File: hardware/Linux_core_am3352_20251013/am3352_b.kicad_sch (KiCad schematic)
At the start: 1 part, among them U1 AM3352BZCZ100

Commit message: update
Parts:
- added C22: 0.1uF, symbol Device:C_Small
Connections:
- net MCASP0_ACLKX: now reaches U1.A13 (MCASP0_ACLKX)
- net MCASP0_AHCLKX: now reaches U1.A14 (MCASP0_AHCLKX)
- net SPI0_CS0: now reaches U1.A16 (SPI0_CS0)
- net SPI0_SCLK: now reaches U1.A17 (SPI0_SCLK)
- net AIN3: now reaches U1.A7 (AIN3)
- net AIN6: now reaches U1.A8 (AIN6)
- net GND: now reaches U1.A9 (VREFN)
- net GND: now also C22.2
- net MCASP0_ACLKR: now reaches U1.B12 (MCASP0_ACLKR)
- net MCASP0_FSX: now reaches U1.B13 (MCASP0_FSX)
- net SPI0_D1: now reaches U1.B16 (SPI0_D1)
- net SPI0_D0: now reaches U1.B17 (SPI0_D0)
- net AIN0: now reaches U1.B6 (AIN0)
- net AIN2: now reaches U1.B7 (AIN2)
- net AIN5: now reaches U1.B8 (AIN5)
- net VDD_ADC: now reaches U1.B9 (VREFP)
- net VDD_ADC: now also C22.1
- net MCASP0_AHCLKR: now reaches U1.C12 (MCASP0_AHCLKR)
- net MCASP0_FSR: now reaches U1.C13 (MCASP0_FSR)
- net SPI0_CS1: now reaches U1.C15 (SPI0_CS1)
- net I2C0_SCL: now reaches U1.C16 (I2C0_SCL)
- net I2C0_SDA: now reaches U1.C17 (I2C0_SDA)
- net ECAP0_IN_PWM0_OUT: now reaches U1.C18 (ECAP0_IN_PWM0_OUT)
- net PMIC_NWAKEUP: now reaches U1.C5 (EXT_WAKEUP)
- net PMIC_POWER_EN: now reaches U1.C6 (PMIC_POWER_EN)
- net AIN1: now reaches U1.C7 (AIN1)
- net AIN4: now reaches U1.C8 (AIN4)
- net AIN7: now reaches U1.C9 (AIN7)
- net MCASP0_AXR0: now reaches U1.D12 (MCASP0_AXR0)
- net MCASP0_AXR1: now reaches U1.D13 (MCASP0_AXR1)
- net UART1_TXD: now reaches U1.D15 (UART1_TXD)
- net UART1_RXD: now reaches U1.D16 (UART1_RXD)
- net UART1_RTS_N: now reaches U1.D17 (UART1_RTS_N)
- net UART1_CTS_N: now reaches U1.D18 (UART1_CTS_N)
- net UART0_RXD: now reaches U1.E15 (UART0_RXD)
- net UART0_TXD: now reaches U1.E16 (UART0_TXD)
- net UART0_RTS_N: now reaches U1.E17 (UART0_RTS_N)
- net UART0_CTS_N: now reaches U1.E18 (UART0_CTS_N)
- net USB1_DRVVBUS: now reaches U1.F15 (USB1_DRVVBUS)
- net USB0_DRVVBUS: now reaches U1.F16 (USB0_DRVVBUS)
- net MII1_COL: now reaches U1.H16 (MII1_COL)
- net MII1_CRS: now reaches U1.H17 (MII1_CRS)
- net RMII1_REF_CLK: now reaches U1.H18 (RMII1_REF_CLK)
- net MII1_RX_ER: now reaches U1.J15 (MII1_RX_ER)
- net MII1_TX_EN: now reaches U1.J16 (MII1_TX_EN)
- net MII1_RX_DV: now reaches U1.J17 (MII1_RX_DV)
- net MII1_TXD3: now reaches U1.J18 (MII1_TXD3)
- net MII1_TXD2: now reaches U1.K15 (MII1_TXD2)
- net MII1_TXD1: now reaches U1.K16 (MII1_TXD1)
- net MII1_TXD0: now reaches U1.K17 (MII1_TXD0)
- net MII1_TX_CLK: now reaches U1.K18 (MII1_TX_CLK)
- net MII1_RXD1: now reaches U1.L15 (MII1_RXD1)
- net MII1_RXD2: now reaches U1.L16 (MII1_RXD2)
- net MII1_RXD3: now reaches U1.L17 (MII1_RXD3)
- net MII1_RX_CLK: now reaches U1.L18 (MII1_RX_CLK)
- net USB0_CE: now reaches U1.M15 (USB0_CE)
- net MII1_RXD0: now reaches U1.M16 (MII1_RXD0)
- net MDIO: now reaches U1.M17 (MDIO)
- net MDC: now reaches U1.M18 (MDC)
- net USB0_DP: now reaches U1.N17 (USB0_DP)
- net USB0_DM: now reaches U1.N18 (USB0_DM)
- net USB0_VBUS: now reaches U1.P15 (USB0_VBUS)
- net USB0_ID: now reaches U1.P16 (USB0_ID)
- net USB1_ID: now reaches U1.P17 (USB1_ID)
- net USB1_CE: now reaches U1.P18 (USB1_CE)
- net LCD_DATA0: now reaches U1.R1 (LCD_DATA0)
- net USB1_DP: now reaches U1.R17 (USB1_DP)
- net USB1_DM: now reaches U1.R18 (USB1_DM)
- net LCD_DATA1: now reaches U1.R2 (LCD_DATA1)
- net LCD_DATA2: now reaches U1.R3 (LCD_DATA2)
- net LCD_DATA3: now reaches U1.R4 (LCD_DATA3)
- net LCD_HSYNC: now reaches U1.R5 (LCD_HSYNC)
- net LCD_AC_BIAS_EN: now reaches U1.R6 (LCD_AC_BIAS_EN)
- net LCD_DATA4: now reaches U1.T1 (LCD_DATA4)
- net USB1_VBUS: now reaches U1.T18 (USB1_VBUS)
- net LCD_DATA5: now reaches U1.T2 (LCD_DATA5)
- net LCD_DATA6: now reaches U1.T3 (LCD_DATA6)
- net LCD_DATA7: now reaches U1.T4 (LCD_DATA7)
- net LCD_DATA15: now reaches U1.T5 (LCD_DATA15)
- net LCD_DATA8: now reaches U1.U1 (LCD_DATA8)
- net LCD_DATA9: now reaches U1.U2 (LCD_DATA9)
- net LCD_DATA10: now reaches U1.U3 (LCD_DATA10)
- net LCD_DATA11: now reaches U1.U4 (LCD_DATA11)
- net LCD_VSYNC: now reaches U1.U5 (LCD_VSYNC)
- net LCD_DATA12: now reaches U1.V2 (LCD_DATA12)
- net LCD_DATA13: now reaches U1.V3 (LCD_DATA13)
- net LCD_DATA14: now reaches U1.V4 (LCD_DATA14)
- net LCD_PCLK: now reaches U1.V5 (LCD_PCLK)

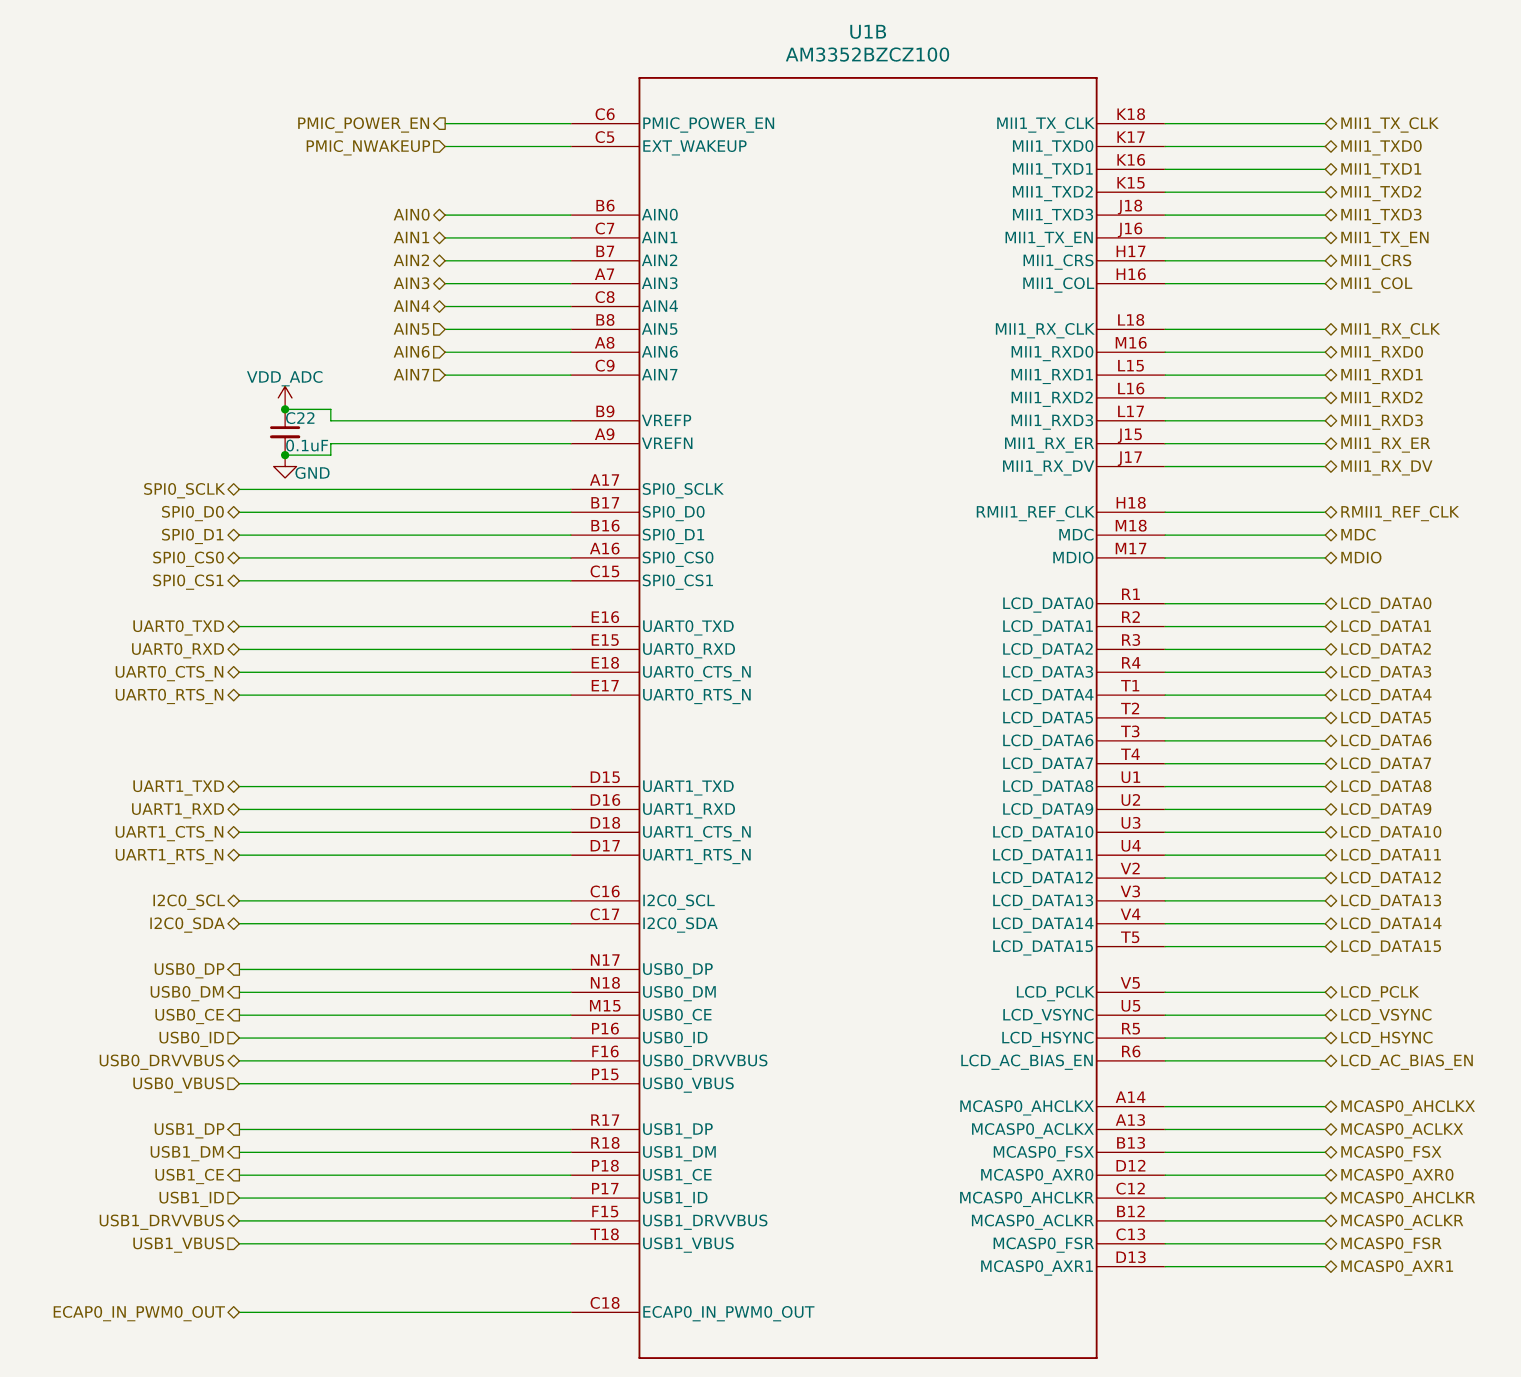
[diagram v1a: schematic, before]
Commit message: update schematic diagram
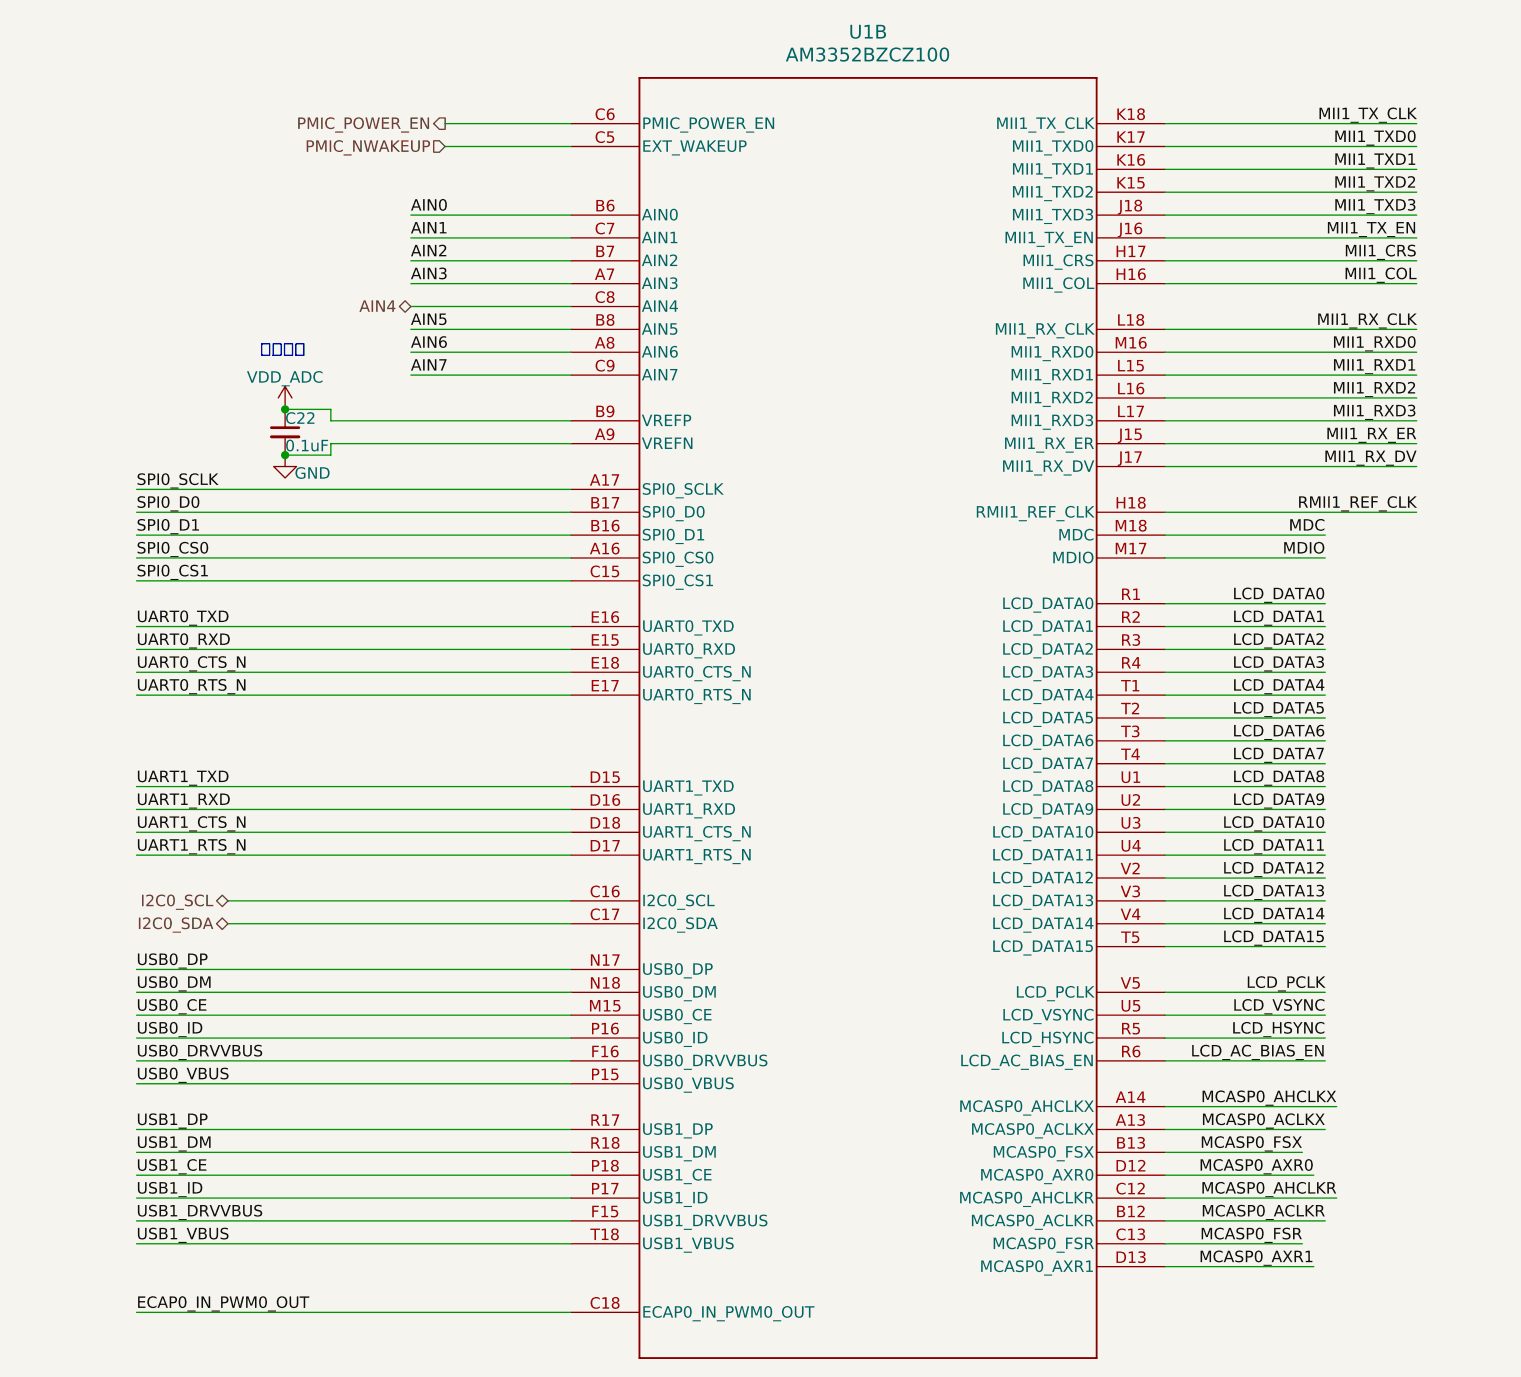
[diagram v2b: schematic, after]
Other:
- note added: "需要更改"
